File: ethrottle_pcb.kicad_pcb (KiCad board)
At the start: 2 copper layers, 35.1 x 54.7 mm, 53 parts, among them J1 ATM15-08PA-BM02, Q1 ZXTR2105F-7, U1 MCP6004, U2 MCP6004, U3 MCP6004, U4 UB2-5NUN

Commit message: finished routing
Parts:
- added H1: MountingHole_Pad, MountingHole:MountingHole_3.5mm_Pad, F.Cu at (92.2, 95.4)
- added H2: MountingHole_Pad, MountingHole:MountingHole_3.5mm_Pad, F.Cu at (92.2, 52.0)
- added H3: MountingHole_Pad, MountingHole:MountingHole_3.5mm_Pad, F.Cu at (137.8, 52.0)
- added H4: MountingHole_Pad, MountingHole:MountingHole_3.5mm_Pad, F.Cu at (137.8, 95.4)
- moved U3 80.3 mm to (105.6, 95.3), turned to 180 degrees
- moved C1 70.6 mm to (112.1, 95.7)
- moved C4 65.6 mm to (110.7, 94.5)
- moved Q1 55.5 mm to (114.5, 82.4)
- moved U1 54.9 mm to (116.8, 95.2)
- moved R14 44.8 mm to (113.8, 98.8), turned to 180 degrees
- moved R18 42.5 mm to (106.5, 99.3), turned to 180 degrees
- moved D12 42.0 mm to (100.6, 89.9)
- moved D16 40.8 mm to (99.8, 60.9), turned to 90 degrees
- moved C5 40.6 mm to (111.7, 88.5), turned to 0 degrees
- moved R24 40.6 mm to (98.5, 95.0), turned to 90 degrees
- moved R17 40.1 mm to (106.5, 98.4), turned to 0 degrees
- moved R25 40.0 mm to (99.7, 95.0), turned to -90 degrees
- moved U2 40.0 mm to (124.5, 78.4)
- moved U4 39.5 mm to (104.0, 69.2)
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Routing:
- net TREF: track 0.00 -> 93.5 mm, vias 0 -> 2
- net BREF: track 0.00 -> 73.3 mm
- net Net-(D12-Pad2): track 0.00 -> 65.7 mm, vias 0 -> 2
- net +5V: track 0.00 -> 62.8 mm, vias 0 -> 6
- net Brake: track 0.00 -> 59.0 mm, vias 0 -> 1
- net Net-(R24-Pad2): track 0.00 -> 56.2 mm, vias 0 -> 4
- net GND: track 0.00 -> 53.8 mm, vias 0 -> 19
- net 4.5V: track 0.00 -> 48.0 mm, vias 0 -> 4
- net Throttle: track 0.00 -> 40.9 mm, vias 0 -> 3
- net +12V: track 0.00 -> 39.7 mm
- net Net-(C2-Pad1): track 0.00 -> 37.2 mm
- net Net-(D16-Pad1): track 0.00 -> 36.3 mm, vias 0 -> 2
- net Net-(C5-Pad1): track 0.00 -> 24.0 mm, vias 0 -> 3
- net Net-(R13-Pad2): track 0.00 -> 21.1 mm, vias 0 -> 2
- net 0.5V: track 0.00 -> 19.9 mm, vias 0 -> 2
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- added copper zone on F.Cu, net +5V
- added copper zone on B.Cu, net GND
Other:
- board size 35.1 x 54.7 mm -> 59 x 56.4 mm

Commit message: layout edits
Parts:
- added TP1: TREF-Test, TestPoint:TestPoint_Plated_Hole_D2.0mm, F.Cu at (92.2, 68.1)
- added TP2: BREF-Test, TestPoint:TestPoint_Plated_Hole_D2.0mm, F.Cu at (115.2, 60.0)
- moved R6 33.1 mm to (92.3, 81.9), turned to 90 degrees
- moved R1 30.3 mm to (92.3, 74.3), turned to 90 degrees
- moved H2 8.01 mm to (92.2, 60.0)
- moved H3 8.01 mm to (137.8, 60.0)
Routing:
- net TREF: track 93.5 -> 63.4 mm
- net BREF: track 73.3 -> 79.0 mm
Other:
- board size 59 x 56.4 mm -> 59 x 48 mm

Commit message: adjust traces
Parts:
- moved R11 12.5 mm to (133.9, 75.2)
- moved D10 10.3 mm to (138.7, 71.5)
- moved D5 10.3 mm to (132.1, 73.3)
- moved D9 10.3 mm to (135.1, 71.4)
- moved U2 9.43 mm to (127.0, 69.3)
- moved D13 5.98 mm to (135.6, 66.7)
- moved C1 0.69 mm to (112.5, 96.3), turned to -90 degrees
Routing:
- net +5V: track 62.8 -> 24.9 mm, vias 6 -> 2
- net Throttle: track 40.9 -> 69.2 mm, vias 3 -> 4
- net 4.5V: track 48.0 -> 69.3 mm
- net Net-(R24-Pad2): track 56.2 -> 75.2 mm, vias 4 -> 6
- net Net-(D13-Pad1): track 16.0 -> 28.7 mm
- net Net-(D9-Pad2): track 7.37 -> 19.6 mm, vias 0 -> 2
- net Brake: track 59.0 -> 69.5 mm, vias 1 -> 2
- net Net-(D10-Pad2): track 16.7 -> 27.2 mm
- net 0.5V: track 19.9 -> 29.5 mm, vias 2 -> 4
- net Net-(D12-Pad2): track 65.7 -> 72.1 mm
- net Net-(D14-Pad2): track 4.10 -> 9.77 mm
- net Net-(D5-Pad2): track 1.12 -> 3.61 mm
- net GND: track 53.8 -> 56.1 mm, vias 19 -> 18
- net TREF: track 63.4 -> 64.8 mm

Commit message: silkscreen
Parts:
- renumbered TP2 to BREF, TP1 to TREF
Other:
- board text added: "SCR2023 BSPD"
- board text added: "\"

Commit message: silkscreen
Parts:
- renumbered TREF to TP1, BREF to TP2
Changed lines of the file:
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@@
       (effects (font (size 1 1) (thickness 0.15)))
     )
-    (fp_text user "*" (at 0 0) (layer "F.SilkS")
+    (fp_text user "*" (at 0 0) (layer "F.SilkS") hide
       (effects (font (size 1 1) (thickness 0.15)))
     )
@@
     (property "Sheetname" "")
     (attr exclude_from_pos_files)
-    (fp_text reference "BREF" (at 0 -2.498) (layer "F.SilkS")
+    (fp_text reference "TP2" (at 0 -2.498) (layer "F.SilkS")
       (effects (font (size 1 1) (thickness 0.15)))
     )
@@
       (effects (font (size 1 1) (thickness 0.15)))
     )
-    (fp_text user "*" (at 0 0) (layer "F.SilkS")
+    (fp_text user "*" (at 0 0) (layer "F.SilkS") hide
       (effects (font (size 1 1) (thickness 0.15)))
     )
@@
     (property "Sheetname" "")
     (attr exclude_from_pos_files)
-    (fp_text reference "TREF" (at 0 -2.498) (layer "F.SilkS")
+    (fp_text reference "TP1" (at 0 -2.498) (layer "F.SilkS")
       (effects (font (size 1 1) (thickness 0.15)))
     )
@@
   (segment (start 129.8394 77.4894) (end 129.8394 71.2758) (width 0.1397) (layer "F.Cu") (net 32))
   (segment (start 131.41 79.06) (end 129.8394 77.4894) (width 0.1397) (layer "F.Cu") (net 32))
-  (segment (start 131.3958 80.3658) (end 131.41 80.38) (width 0.1397) (layer "F.Cu") (net 32))
-  (segment (start 131.41 80.38) (end 131.41 79.06) (width 0.1397) (layer "F.Cu") (net 32))
+  (segment (start 131.41 79.06) (end 131.41 80.38) (width 0.1397) (layer "F.Cu") (net 32))
   (segment (start 107.52 77.25) (end 107.54 77.27) (width 0.1397) (layer "F.Cu") (net 33))
   (segment (start 107.52 76.175) (end 107.52 77.25) (width 0.1397) (layer "F.Cu") (net 33))
@@
   (segment (start 117.26 84.85) (end 115.9525 84.85) (width 0.1397) (layer "F.Cu") (net 34))
   (segment (start 115.93 84.8275) (end 115.93 85.8325) (width 0.1397) (layer "F.Cu") (net 34))
-  (segment (start 119.42 82.07) (end 119.42 82.69) (width 0.1397) (layer "F.Cu") (net 34))
+  (segment (start 119.42 82.69) (end 119.42 81.84) (width 0.1397) (layer "F.Cu") (net 34))
   (segment (start 125.85 68.97) (end 125.5396 68.6596) (width 0.1397) (layer "F.Cu") (net 34))
   (segment (start 127.28 69.07) (end 125.95 69.07) (width 0.1397) (layer "F.Cu") (net 34))
@@
   (segment (start 115.9525 84.85) (end 115.93 84.8275) (width 0.1397) (layer "F.Cu") (net 34))
   (via (at 124.99 77.12) (size 0.56) (drill 0.3) (layers "F.Cu" "B.Cu") (net 34))
+  (via (at 119.42 81.84) (size 0.56) (drill 0.3) (layers "F.Cu" "B.Cu") (net 34))
   (via (at 127.28 69.07) (size 0.56) (drill 0.3) (layers "F.Cu" "B.Cu") (net 34))
-  (via (at 119.42 82.07) (size 0.56) (drill 0.3) (layers "F.Cu" "B.Cu") (net 34))
   (via (at 125.56 72.89) (size 0.56) (drill 0.3) (layers "F.Cu" "B.Cu") (net 34))
-  (segment (start 119.42 82.07) (end 124.37 77.12) (width 0.1397) (layer "B.Cu") (net 34))
-  (segment (start 124.37 77.12) (end 124.99 77.12) (width 0.1397) (layer "B.Cu") (net 34))
-  (segment (start 119.39 82.07) (end 119.42 82.07) (width 0.1397) (layer "B.Cu") (net 34))
+  (segment (start 119.42 81.84) (end 124.14 77.12) (width 0.1397) (layer "B.Cu") (net 34))
+  (segment (start 124.14 77.12) (end 124.99 77.12) (width 0.1397) (layer "B.Cu") (net 34))
   (segment (start 126.55 71.9) (end 127.15 71.9) (width 0.1397) (layer "B.Cu") (net 34))
   (segment (start 125.56 72.89) (end 126.55 71.9) (width 0.1397) (layer "B.Cu") (net 34))

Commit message: small change
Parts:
- moved C1 37.5 mm to (140.7, 120.9)
- moved C2 37.5 mm to (159.4, 120.5)
- moved C3 37.5 mm to (158.7, 109.6)
- moved C4 37.5 mm to (139.0, 119.1)
- moved D1 37.5 mm to (140.4, 116.3)
- moved D10 37.5 mm to (166.9, 96.0)
- moved D12 37.5 mm to (128.8, 114.5)
- moved D14 37.5 mm to (159.7, 103.3)
- moved D16 37.5 mm to (128.1, 85.5)
- moved D2 37.5 mm to (140.6, 123.0)
- moved D3 37.5 mm to (149.5, 123.4)
- moved D5 37.5 mm to (160.3, 97.9)
- moved D9 37.5 mm to (163.4, 96.0)
- moved H3 37.5 mm to (166.1, 84.6)
- moved H4 37.5 mm to (166.1, 120.0)
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
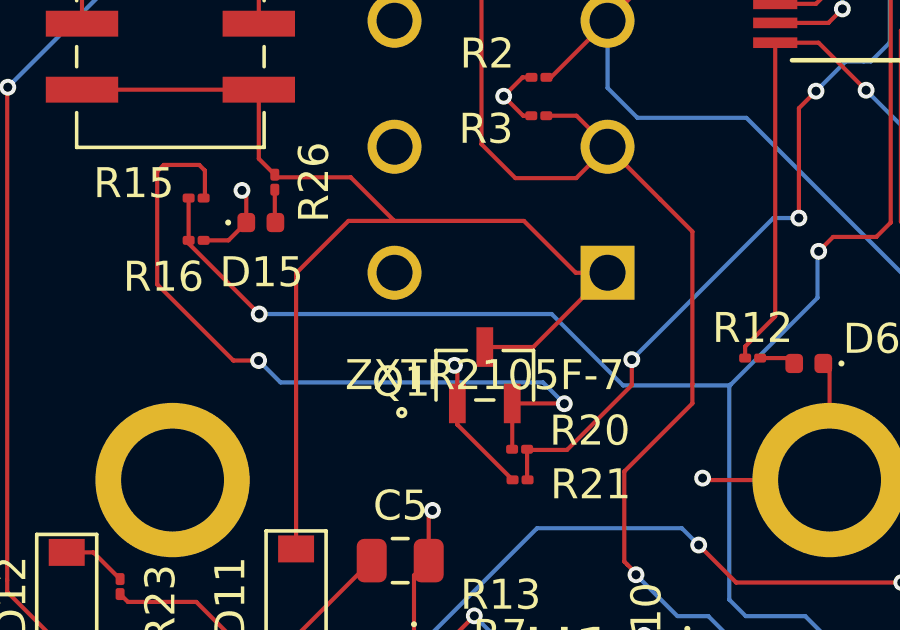
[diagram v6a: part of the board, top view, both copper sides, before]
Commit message: add decoupling capacitor
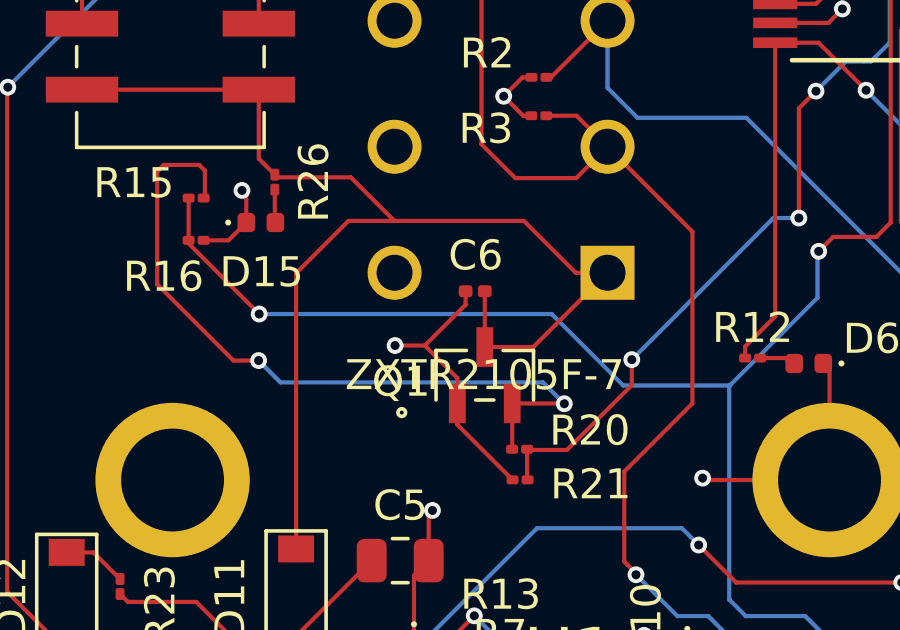
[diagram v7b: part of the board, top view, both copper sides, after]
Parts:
- added C6: 1uF, Capacitor_SMD:C_0201_0603Metric, F.Cu at (142.4, 104.2)
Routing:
- net GND: track 56.1 -> 60.5 mm
- net +12V: track 39.7 -> 41.6 mm
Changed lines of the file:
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@@
+  )
+  (footprint "Capacitor_SMD:C_0201_0603Metric" (layer "F.Cu")
+    (at 142.44 104.16 180)
+    (descr "Capacitor SMD 0201 (0603 Metric), square (rectangular) end terminal, IPC_7351 nominal, (Body size source: https://www.vishay.com/docs/20052/crcw0201e3.pdf), generated with kicad-footprint-generator")
+    (tags "capacitor")
+    (property "Sheetfile" "ethrottle_pcb.kicad_sch")
+    (property "Sheetname" "")
+    (attr smd)
+    (fp_text reference "C6" (at -0.02 1.19) (layer "F.SilkS")
+      (effects (font (size 1 1) (thickness 0.15)))
+    )
+    (fp_text value "1uF" (at 0 1.05) (layer "F.Fab")
+      (effects (font (size 1 1) (thickness 0.15)))
+    )
+    (fp_text user "${REFERENCE}" (at 0 -0.68) (layer "F.Fab")
+      (effects (font (size 0.25 0.25) (thickness 0.04)))
+    )
+    (fp_line (start 0.7 0.35) (end -0.7 0.35) (layer "F.CrtYd") (width 0.05))
+    (fp_line (start 0.7 -0.35) (end 0.7 0.35) (layer "F.CrtYd") (width 0.05))
+    (fp_line (start -0.7 -0.35) (end 0.7 -0.35) (layer "F.CrtYd") (width 0.05))
+    (fp_line (start -0.7 0.35) (end -0.7 -0.35) (layer "F.CrtYd") (width 0.05))
+    (fp_line (start 0.3 -0.15) (end 0.3 0.15) (layer "F.Fab") (width 0.1))
+    (fp_line (start 0.3 0.15) (end -0.3 0.15) (layer "F.Fab") (width 0.1))
+    (fp_line (start -0.3 -0.15) (end 0.3 -0.15) (layer "F.Fab") (width 0.1))
+    (fp_line (start -0.3 0.15) (end -0.3 -0.15) (layer "F.Fab") (width 0.1))
+    (pad "" smd roundrect (at -0.345 0 180) (size 0.318 0.36) (layers "F.Paste") (roundrect_rratio 0.25))
+    (pad "" smd roundrect (at 0.345 0 180) (size 0.318 0.36) (layers "F.Paste") (roundrect_rratio 0.25))
+    (pad "1" smd roundrect (at -0.32 0 180) (size 0.46 0.4) (layers "F.Cu" "F.Mask") (roundrect_rratio 0.25)
+      (net 28 "+12V") (pintype "passive"))
+    (pad "2" smd roundrect (at 0.32 0 180) (size 0.46 0.4) (layers "F.Cu" "F.Mask") (roundrect_rratio 0.25)
+      (net 2 "GND") (pintype "passive"))
+    (model "${KICAD6_3DMODEL_DIR}/Capacitor_SMD.3dshapes/C_0201_0603Metric.wrl"
+      (offset (xyz 0 0 0))
+      (scale (xyz 1 1 1))
+      (rotate (xyz 0 0 0))
+    )
   )
   (footprint "Capacitor_SMD:C_0201_0603Metric" (layer "F.Cu")
@@
   (segment (start 134.216 102.464) (end 134.81 101.87) (width 0.1397) (layer "F.Cu") (net 2))
   (segment (start 121.55 108.33) (end 121.55 109.816) (width 0.1397) (layer "F.Cu") (net 2))
+  (segment (start 141.845001 107.055001) (end 140.76 105.97) (width 0.1397) (layer "F.Cu") (net 2))
   (segment (start 140.59 123.535) (end 139.617 123.535) (width 0.1397) (layer "F.Cu") (net 2))
   (segment (start 135.2264 86.9084) (end 132.352 84.034) (width 0.1397) (layer "F.Cu") (net 2))
   (segment (start 134.81 101.87) (end 134.81 100.944) (width 0.1397) (layer "F.Cu") (net 2))
+  (segment (start 142.12 104.61) (end 140.76 105.97) (width 0.1397) (layer "F.Cu") (net 2))
   (segment (start 132.128 83.81) (end 132.352 84.034) (width 0.1397) (layer "F.Cu") (net 2))
   (segment (start 140.4 115.865) (end 140.4 113.63) (width 0.1397) (layer "F.Cu") (net 2))
@@
   (segment (start 139.492 123.66) (end 139.492 122.423) (width 0.1397) (layer "F.Cu") (net 2))
   (segment (start 154.043 106.568) (end 154.252 106.777) (width 0.1397) (layer "F.Cu") (net 2))
+  (segment (start 141.845001 107.8998) (end 141.845001 107.055001) (width 0.1397) (layer "F.Cu") (net 2))
   (segment (start 150.34875 122.89125) (end 150.61 122.63) (width 0.1397) (layer "F.Cu") (net 2))
   (segment (start 128.812 119.862) (end 128.824 119.85) (width 0.1397) (layer "F.Cu") (net 2))
   (segment (start 158.72 109.28) (end 158.72 108.28) (width 0.1397) (layer "F.Cu") (net 2))
   (segment (start 159.41 121.47) (end 159.41 122.71) (width 0.1397) (layer "F.Cu") (net 2))
+  (segment (start 140.76 105.97) (end 139.77 105.97) (width 0.1397) (layer "F.Cu") (net 2))
   (segment (start 128.864 119.89) (end 128.824 119.85) (width 0.1397) (layer "F.Cu") (net 2))
   (segment (start 131.0406 119.89) (end 128.864 119.89) (width 0.1397) (layer "F.Cu") (net 2))
@@
   (segment (start 159.41 122.71) (end 159.28 122.84) (width 0.1397) (layer "F.Cu") (net 2))
   (segment (start 133.44 123.87) (end 133.396 123.914) (width 0.1397) (layer "F.Cu") (net 2))
-  (segment (start 141.845001 107.8998) (end 141.845001 106.725001) (width 0.1397) (layer "F.Cu") (net 2))
   (segment (start 147.8994 119.85) (end 149.398 119.85) (width 0.1397) (layer "F.Cu") (net 2))
   (segment (start 139.304 117.996) (end 139.34 117.96) (width 0.1397) (layer "F.Cu") (net 2))
   (segment (start 140.89 111.594) (end 141.016 111.468) (width 0.1397) (layer "F.Cu") (net 2))
-  (segment (start 141.845001 106.725001) (end 141.75 106.63) (width 0.1397) (layer "F.Cu") (net 2))
   (segment (start 158.72 108.28) (end 158.71 108.27) (width 0.1397) (layer "F.Cu") (net 2))
   (segment (start 139.617 123.535) (end 139.492 123.66) (width 0.1397) (layer "F.Cu") (net 2))
@@
   (segment (start 133.388 102.464) (end 134.216 102.464) (width 0.1397) (layer "F.Cu") (net 2))
   (segment (start 144.315 97.03) (end 144.02 97.03) (width 0.1397) (layer "F.Cu") (net 2))
+  (segment (start 142.12 104.16) (end 142.12 104.61) (width 0.1397) (layer "F.Cu") (net 2))
   (segment (start 149.46 122.89125) (end 150.34875 122.89125) (width 0.1397) (layer "F.Cu") (net 2))
   (segment (start 139.304 119.088) (end 139.304 117.996) (width 0.1397) (layer "F.Cu") (net 2))
@@
   (via (at 159.63 93.92) (size 0.56) (drill 0.3) (layers "F.Cu" "B.Cu") (net 2))
   (via (at 158.71 108.27) (size 0.56) (drill 0.3) (layers "F.Cu" "B.Cu") (net 2))
+  (via (at 139.77 105.97) (size 0.56) (drill 0.3) (layers "F.Cu" "B.Cu") (net 2))
   (via (at 121.566 99.164) (size 0.56) (drill 0.3) (layers "F.Cu" "B.Cu") (net 2))
   (via (at 141.016 111.468) (size 0.56) (drill 0.3) (layers "F.Cu" "B.Cu") (net 2))
@@
   (via (at 150.02 110.39) (size 0.56) (drill 0.3) (layers "F.Cu" "B.Cu") (net 2))
   (via (at 149.398 119.85) (size 0.56) (drill 0.3) (layers "F.Cu" "B.Cu") (net 2))
-  (via (at 141.75 106.63) (size 0.56) (drill 0.3) (layers "F.Cu" "B.Cu") (net 2))
   (via (at 160.846 96.798) (size 0.56) (drill 0.3) (layers "F.Cu" "B.Cu") (net 2))
   (via (at 134.666 100.8) (size 0.56) (drill 0.3) (layers "F.Cu" "B.Cu") (net 2))
@@
   (segment (start 139.746 101.816) (end 144.064 101.816) (width 0.1397) (layer "F.Cu") (net 28))
   (segment (start 144.3758 106.0202) (end 146.852 103.544) (width 0.1397) (layer "F.Cu") (net 28))
+  (segment (start 142.76 104.16) (end 142.76 106.0202) (width 0.1397) (layer "F.Cu") (net 28))
   (segment (start 135.76 100.275) (end 135.2264 99.7414) (width 0.1397) (layer "F.Cu") (net 28))
   (segment (start 145.792 103.544) (end 146.852 103.544) (width 0.1397) (layer "F.Cu") (net 28))
